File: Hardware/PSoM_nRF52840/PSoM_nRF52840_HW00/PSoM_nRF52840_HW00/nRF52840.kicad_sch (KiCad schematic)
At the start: 31 parts

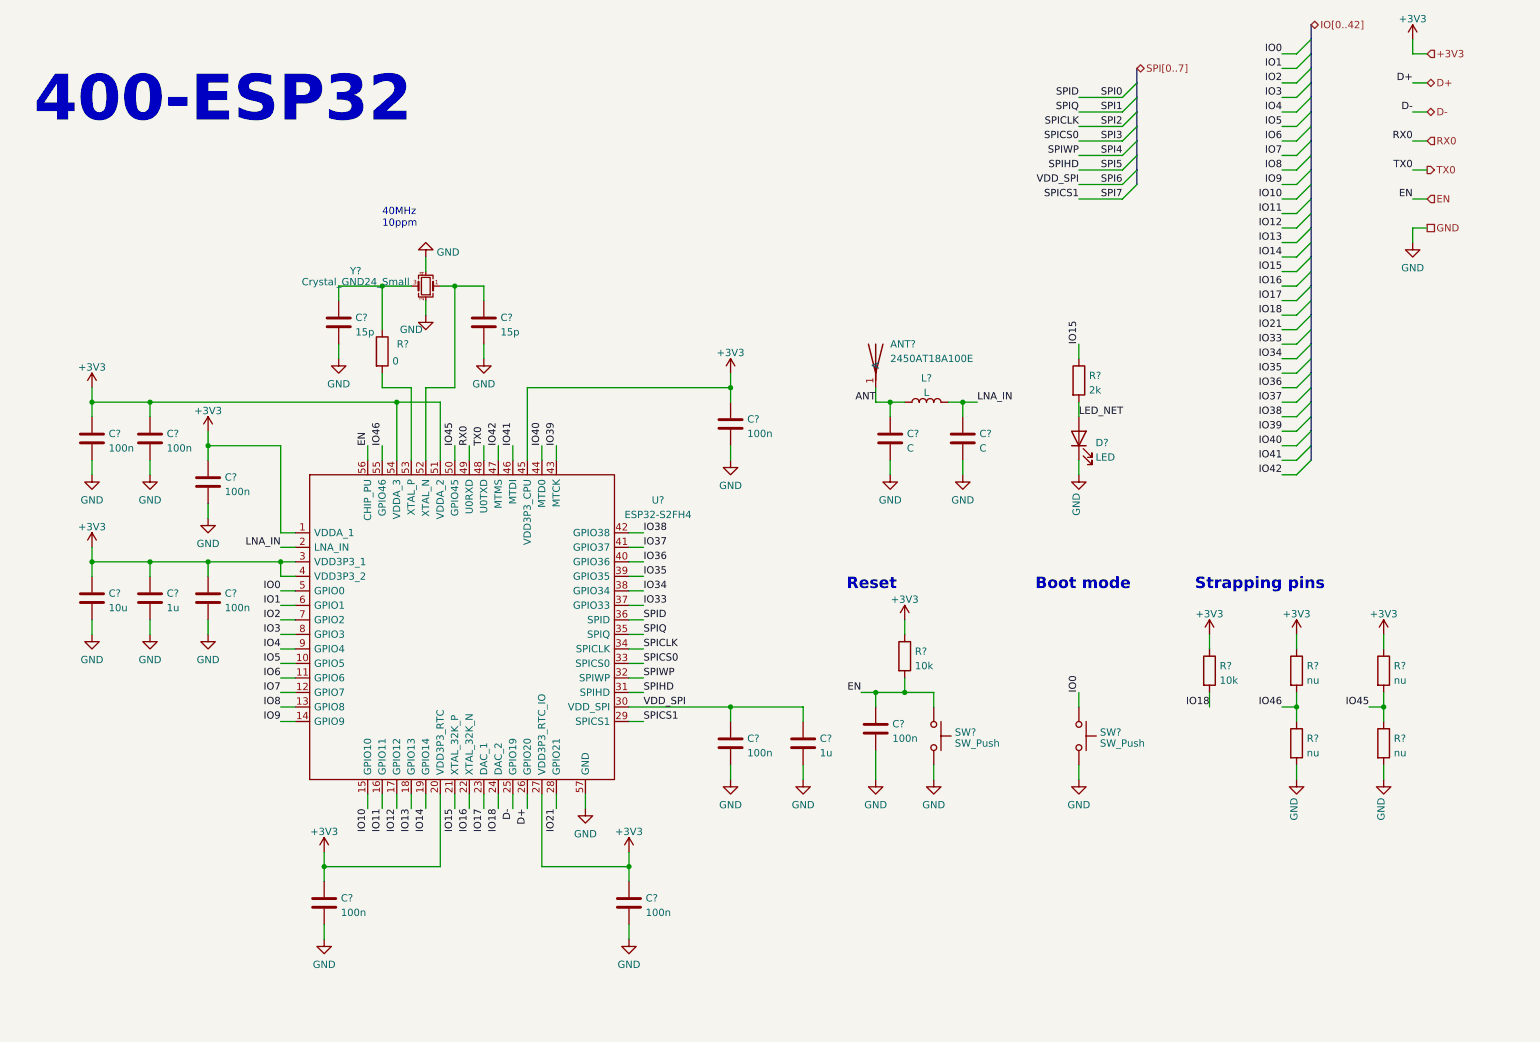
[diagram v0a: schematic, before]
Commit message: nrf schematic ongoing
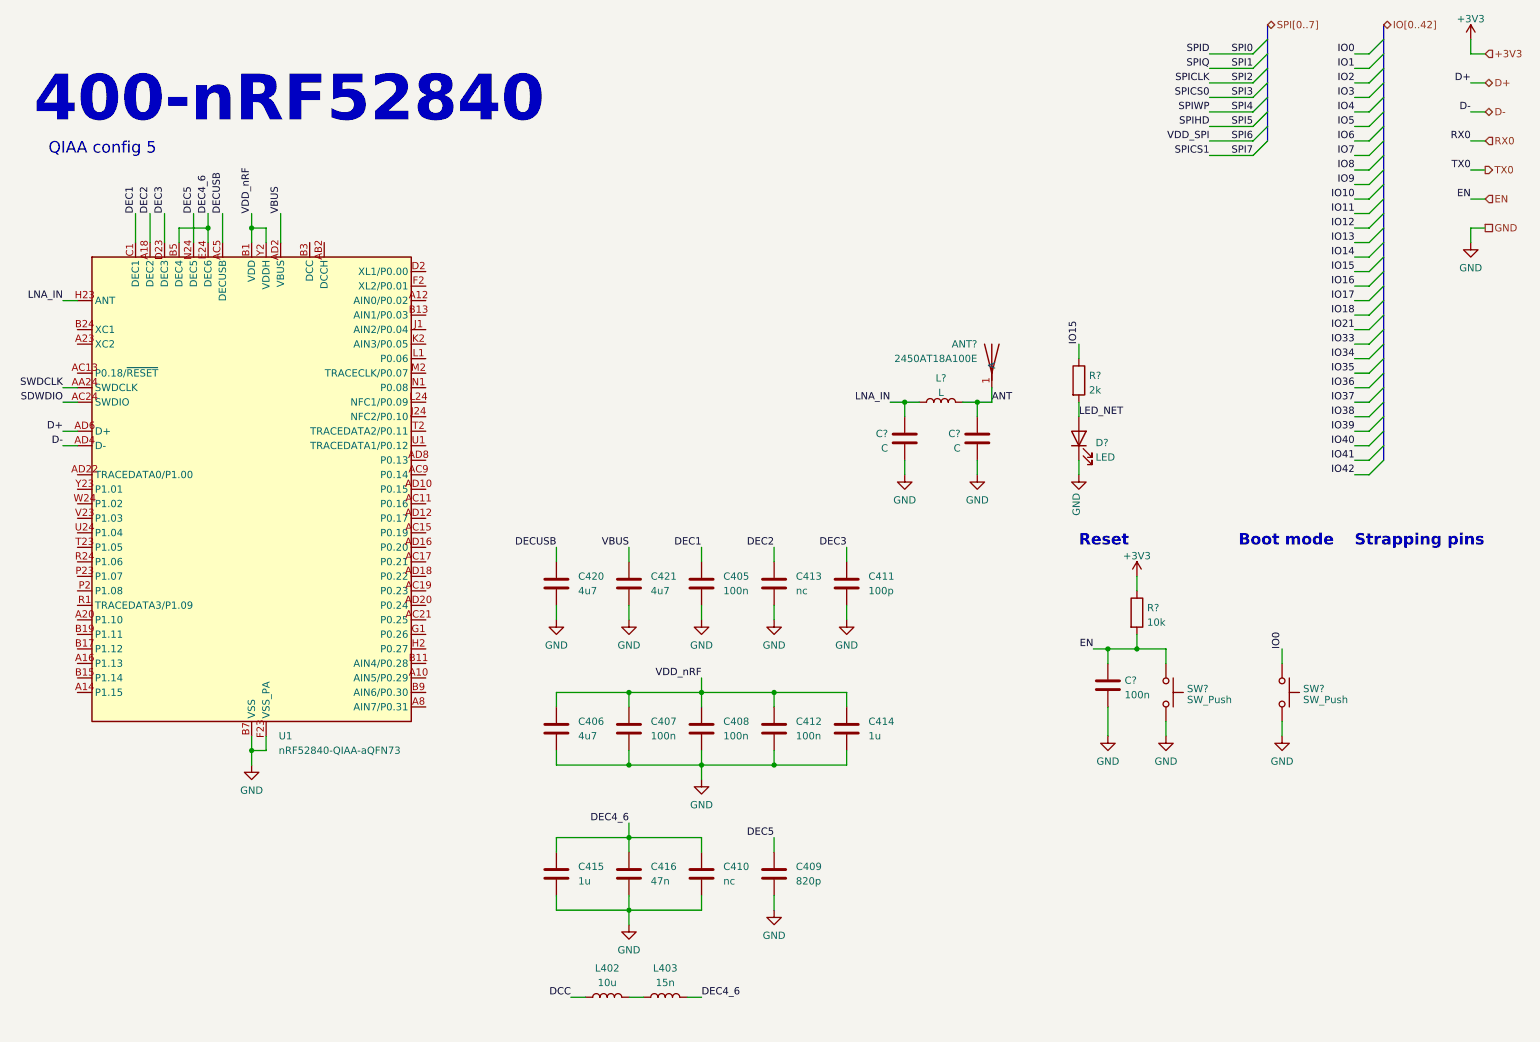
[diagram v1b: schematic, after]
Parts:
- removed C? (x8): 100n, Capacitor_SMD:C_0201_0603Metric, symbol Component lib:C
- removed C? (x2): 15p, Capacitor_SMD:C_0201_0603Metric, symbol Component lib:C
- removed C? (x2): 1u, Capacitor_SMD:C_0402_1005Metric, symbol Component lib:C
- removed C?: 10u, Capacitor_SMD:C_0603_1608Metric, symbol Component lib:C
- removed R? (x4): nu, Resistor_SMD:R_0201_0603Metric, symbol Component lib:R
- removed R?: 10k, Resistor_SMD:R_0201_0603Metric, symbol Component lib:R
- removed R?: 0, Resistor_SMD:R_0201_0603Metric, symbol Component lib:R
- removed U?: ESP32-S2FH4, Component_lib:QFN40P700X700X90-57N-D, symbol Component_lib:ESP32-S2FH4
- removed Y?: Crystal_GND24_Small, Component_lib:Crystal_SMD_2016-4Pin_2.0x1.6mm, symbol Device:Crystal_GND24_Small
- added C405, C407, C408, C412: 100n, symbol Component_lib:C
- added C406, C420, C421: 4u7, symbol Component_lib:C
- added C409: 820p, symbol Component_lib:C
- added C410, C413: nc, symbol Component_lib:C
- added C411: 100p, symbol Component_lib:C
- added C414, C415: 1u, symbol Component_lib:C
- added C416: 47n, symbol Component_lib:C
- added L402: 10u, symbol Component_lib:L
- added L403: 15n, symbol Component_lib:L
- added U1: nRF52840-QIAA-aQFN73, Component_lib:Nordic_AQFN-73-1EP_7x7mm_P0.5mm, symbol Component_lib:nRF52840-QIAA-aQFN73
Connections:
- net D+: now also U1.AD6 (D+)
- net D-: now also U1.AD4 (D-)
- net GND: now also C405.2, C406.2, C407.2, C408.2, C409.2, C410.2, C411.2, C412.2, C413.2, C414.2, C415.2, C416.2, C420.2, C421.2, U1.B7 (VSS), U1.EP (VSS), U1.F23 (VSS_PA)
- net LNA_IN: now also U1.H23 (ANT)
- new net: L402.2, L403.1
- new net DCC: L402.1
- new net DEC1: C405.1, U1.C1 (DEC1)
- new net DEC2: C413.1, U1.A18 (DEC2)
- new net DEC3: C411.1, U1.D23 (DEC3)
- new net DEC4_6: C410.1, C415.1, C416.1, L403.2, U1.B5 (DEC4), U1.E24 (DEC6)
- new net DEC5: C409.1, U1.N24 (DEC5)
- new net DECUSB: C420.1, U1.AC5 (DECUSB)
- new net SDWDIO: U1.AC24 (SWDIO)
- new net SWDCLK: U1.AA24 (SWDCLK)
- new net VBUS: C421.1, U1.AD2 (VBUS)
- new net VDD_nRF: C406.1, C407.1, C408.1, C412.1, C414.1, U1.A22 (VDD), U1.AD14 (VDD), U1.AD23 (VDD), U1.B1 (VDD), U1.W1 (VDD), U1.Y2 (VDDH)
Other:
- note added: "400-nRF52840"
- note added: "QIAA config 5"
- note removed: "400-ESP32"
- note removed: "40MHz 10ppm"
- moved on the sheet: ANT?, C?, L?, R?, SW?

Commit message: added quartz + matching circuit for nrf52 psom
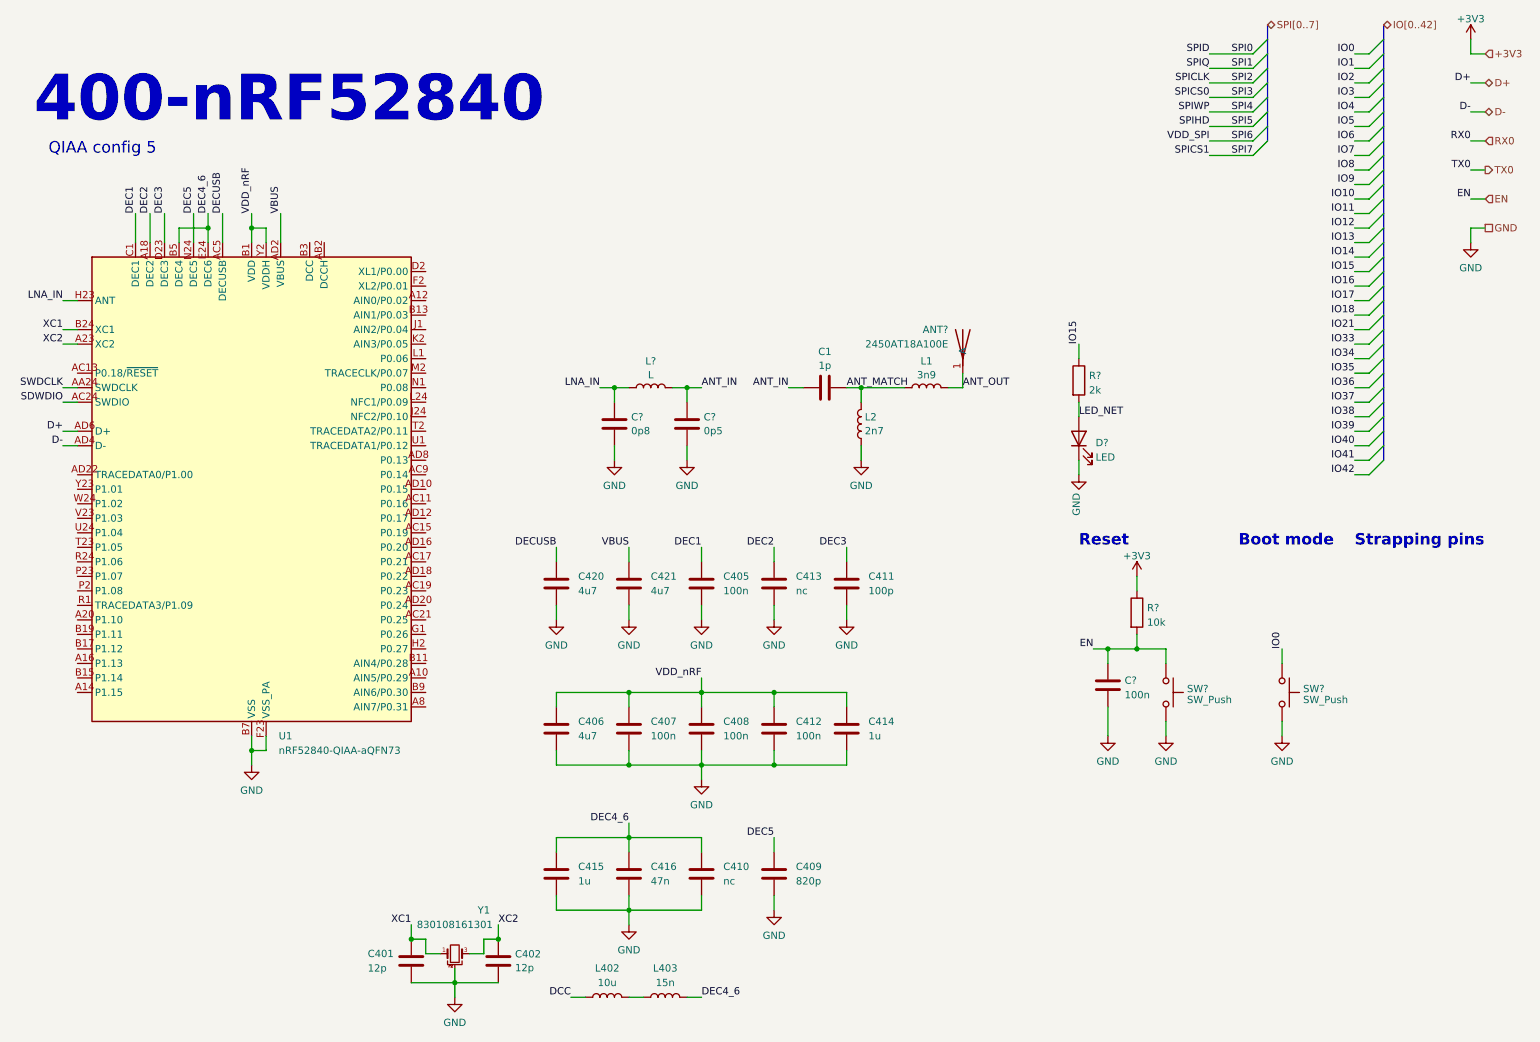
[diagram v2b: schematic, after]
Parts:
- added C1: 1p, Capacitor_SMD:C_0201_0603Metric, symbol Component lib:C
- added C401, C402: 12p, symbol Component_lib:C
- added L1: 3n9, Inductor_SMD:L_0201_0603Metric, symbol Component lib:L
- added L2: 2n7, Inductor_SMD:L_0201_0603Metric, symbol Component lib:L
- added Y1: 830108161301, Component_lib:830108161301_1.6x1.2mm, symbol Component_lib:830108161301
- C?: value C -> 0p8
- C?: value C -> 0p5
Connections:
- net GND: now also C401.2, C402.2, L2.2, Y1.2, Y1.4
- net XC2: now reaches U1.A23 (XC2)
- net XC2: now also C402.1, Y1.3
- net XC1: now reaches U1.B24 (XC1)
- net XC1: now also C401.1, Y1.1
- net ANT renamed ANT_IN
- net ANT_IN: now also C1.2; no longer ANT?.1 (A)
- new net ANT_MATCH: C1.1, L1.2, L2.1
- new net ANT_OUT: ANT?.1 (A), L1.1
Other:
- moved on the sheet: ANT?, C?, L?

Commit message: working on schematic
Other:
- title: PSoM - ESP32 S2 -> PSoM - nRF52840
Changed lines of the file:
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@@
 	(paper "A4")
 	(title_block
-		(title "PSoM - ESP32 S2")
-		(date "2023-04-17")
+		(title "PSoM - nRF52840")
+		(date "2024-09-30")
 		(rev "HW00")
 		(company "PumaCorp")
